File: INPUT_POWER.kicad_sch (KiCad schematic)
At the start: 30 parts, among them J1 TYPE-C-31-M12_13, SW3 ON/OFF, U3 IP5306

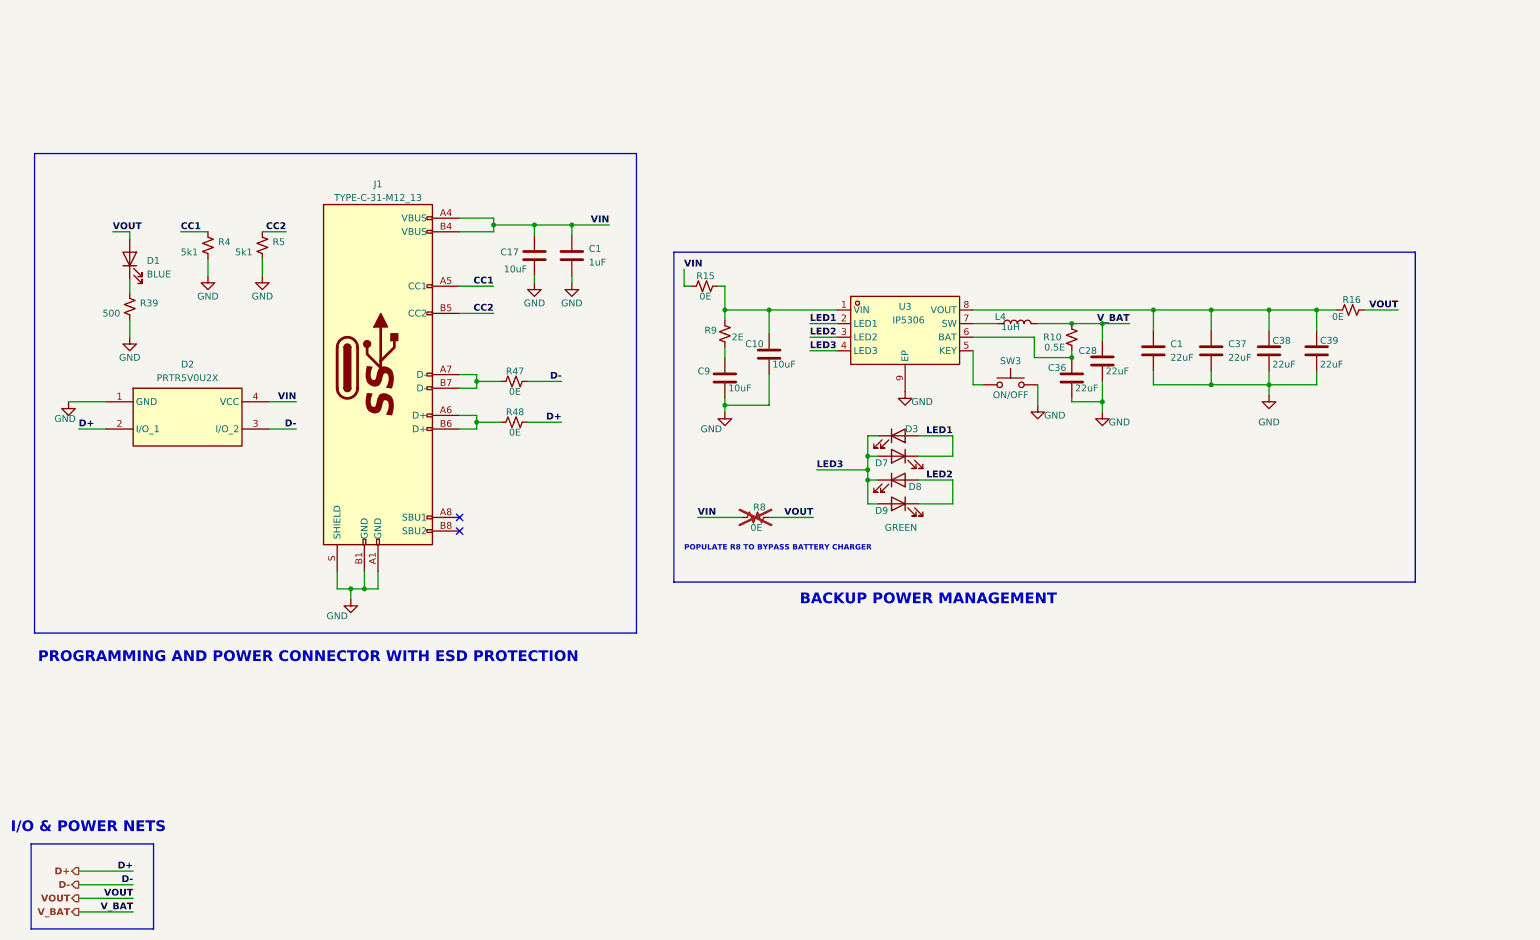
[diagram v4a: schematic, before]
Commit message: Added Arduino style SS for GPIO headers, Added BLE & Wi-Fi symbol
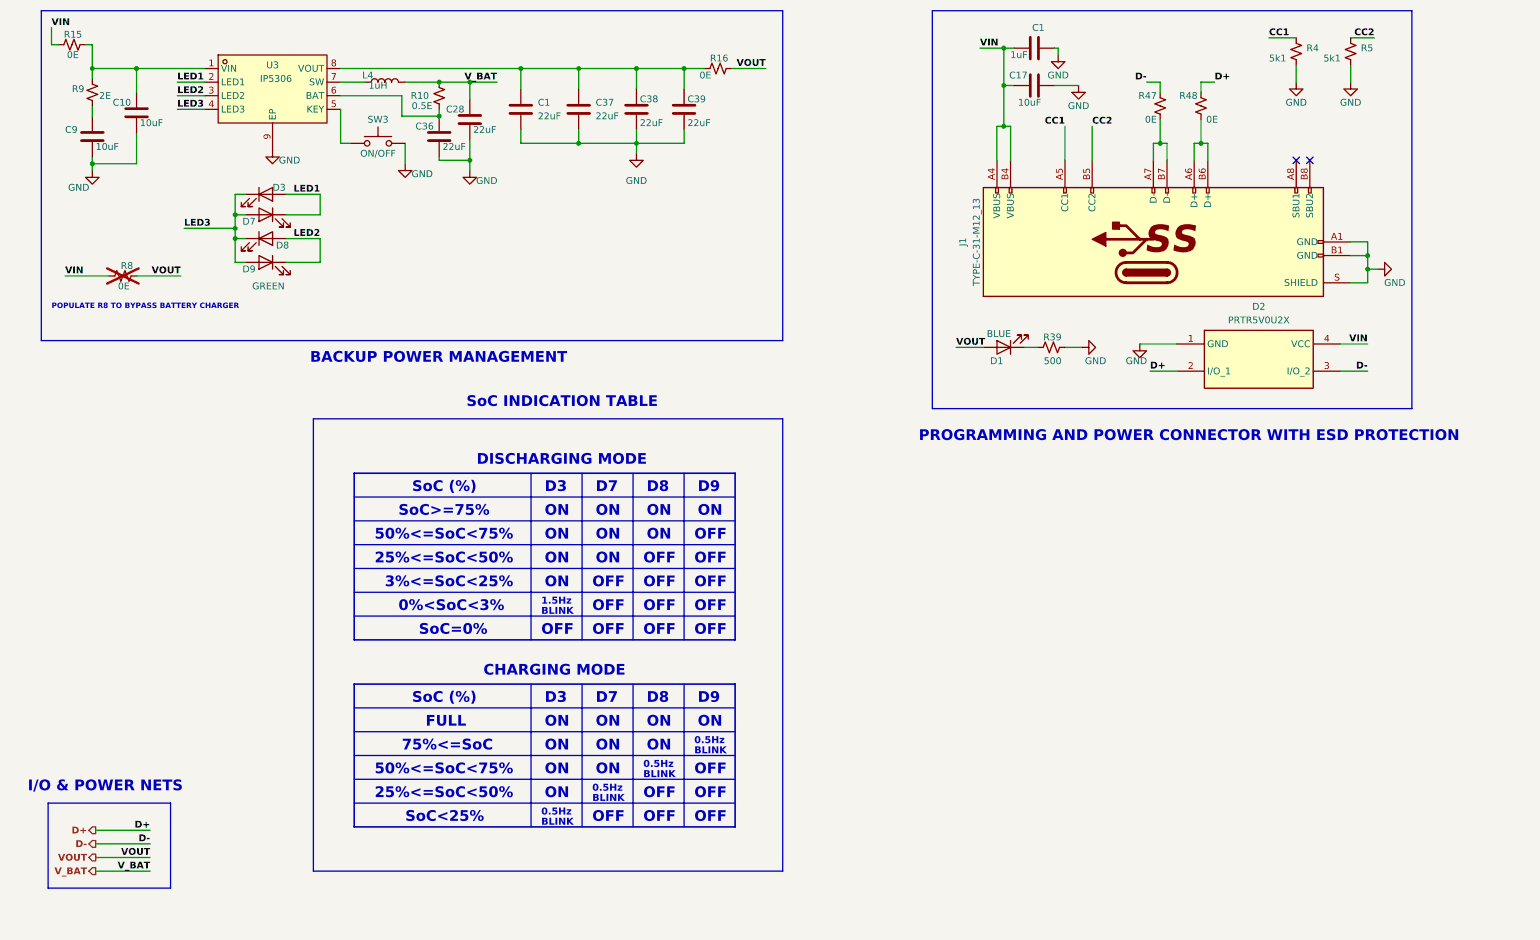
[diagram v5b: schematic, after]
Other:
- note added: "0%<SoC<3%"
- note added: "0.5Hz"
- note added: "1.5Hz"
- note added: "25%<=SoC<50%"
- note added: "3%<=SoC<25%"
- note added: "50%<=SoC<75%"
- note added: "75%<=SoC"
- note added: "BLINK"
- note added: "CHARGING MODE"
- note added: "D3"
- note added: "D7"
- note added: "D8"
- note added: "D9"
- note added: "DISCHARGING MODE"
- note added: "FULL"
- note added: "OFF"
- note added: "ON"
- note added: "SoC (%)"
- note added: "SoC INDICATION TABLE"
- note added: "SoC<25%"
- note added: "SoC=0%"
- note added: "SoC>=75%"
- moved on the sheet: C1, C10, C17, C28, C36, C37, C38, C39, C9, D1, D2, D3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

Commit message: Added HW-Tinkerers logo and supporting graphics
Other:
- company: (none) -> HW-TINKERERS (hw.tinkerers@gmail.com)
- title: (none) -> HARDWARE TINKERERS ESP32-S3 DB
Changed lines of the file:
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@@
 (kicad_sch (version 20230121) (generator eeschema)
   (paper "A4")
+  (title_block
+    (title "HARDWARE TINKERERS ESP32-S3 DB")
+    (rev "1.0.0")
+    (company "HW-TINKERERS (hw.tinkerers@gmail.com)")
+    (comment 1 "Email: bhandarkasrishtikr111@gmail.com")
+    (comment 2 "Author: Srishtik Bhandarkar")
+    (comment 3 "Email: vaibhavkhatri00@gmail.com")
+    (comment 4 "Author: Vaibhav Khatri")
+    (comment 5 "Official HW-Tinkerers email: hw.tinkerers@gmail.com")
+  )
   (junction (at 121.92 41.91) (diameter 0) (color 0 0 0 0)
   )

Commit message: Added production files for JLC (BOM and CPL)
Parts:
- C1: LCSC Part Number (none) -> C14664
- C1, C37, C38, C39: LCSC Part Number (none) -> C12891
- C10, C17, C9: LCSC Part Number (none) -> C15850
- C28, C36: LCSC Part Number (none) -> C2762594
- D1: LCSC Part Number (none) -> C84266
- D2: LCSC Part Number (none) -> C2827688
- D3, D7, D8, D9: LCSC Part Number (none) -> C84264
- L4: LCSC Part Number (none) -> C576540
- R10: LCSC Part Number (none) -> C346785
- R15, R16, R47, R48, R8: LCSC Part Number (none) -> C95177
- R39: LCSC Part Number (none) -> C137970
- R4, R5: LCSC Part Number (none) -> C105872
- R9: LCSC Part Number (none) -> C137886
- SW3: LCSC Part Number (none) -> C92584
- U3: LCSC Part Number (none) -> C181692
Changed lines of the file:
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@@
+      (effects (font (size 1.27 1.27)) hide)
+    )
+    (property "LCSC Part Number" "C14664" (at 207.01 24.13 0)
       (effects (font (size 1.27 1.27)) hide)
     )
@@
       (effects (font (size 1.27 1.27)) hide)
     )
+    (property "LCSC Part Number" "C95177" (at 147.955 27.94 0)
+      (effects (font (size 1.27 1.27)) hide)
+    )
     (pin "1")
     (pin "2")
@@
     )
     (property "PN" "NCD0603C1" (at 63.5 51.435 0)
+      (effects (font (size 1.27 1.27)) hide)
+    )
+    (property "LCSC Part Number" "C84264" (at 63.5 51.435 0)
       (effects (font (size 1.27 1.27)) hide)
     )
@@
       (effects (font (size 1.27 1.27)) hide)
     )
+    (property "LCSC Part Number" "C2827688" (at 233.68 79.375 0)
+      (effects (font (size 1.27 1.27)) hide)
+    )
     (pin "1")
     (pin "2")
@@
       (effects (font (size 1.27 1.27)) hide)
     )
+    (property "LCSC Part Number" "C15850" (at 31.115 40.64 0)
+      (effects (font (size 1.27 1.27)) hide)
+    )
     (pin "1")
     (pin "2")
@@
       (effects (font (size 1.27 1.27)) hide)
     )
+    (property "LCSC Part Number" "C137970" (at 210.185 80.01 0)
+      (effects (font (size 1.27 1.27)) hide)
+    )
     (pin "1")
     (pin "2")
@@
     )
     (property "PN" "CL21A106KAYNNNE" (at 207.01 31.115 0)
+      (effects (font (size 1.27 1.27)) hide)
+    )
+    (property "LCSC Part Number" "C15850" (at 207.01 31.115 0)
       (effects (font (size 1.27 1.27)) hide)
     )
@@
       (effects (font (size 1.27 1.27)) hide)
     )
+    (property "LCSC Part Number" "C84266" (at 201.295 80.01 0)
+      (effects (font (size 1.27 1.27)) hide)
+    )
     (pin "1")
     (pin "2")
@@
     )
     (property "PN" "IP5306" (at 64.77 27.94 0)
+      (effects (font (size 1.27 1.27)) hide)
+    )
+    (property "LCSC Part Number" "C181692" (at 64.77 27.94 0)
       (effects (font (size 1.27 1.27)) hide)
     )
@@
       (effects (font (size 1.27 1.27)) hide)
     )
+    (property "LCSC Part Number" "C2762594" (at 101.6 37.465 0)
+      (effects (font (size 1.27 1.27)) hide)
+    )
     (pin "1")
     (pin "2")
@@
     )
     (property "PN" "CL10A226MO7JZNC" (at 95.885 40.64 0)
+      (effects (font (size 1.27 1.27)) hide)
+    )
+    (property "LCSC Part Number" "C2762594" (at 95.885 40.64 0)
       (effects (font (size 1.27 1.27)) hide)
     )
@@
       (effects (font (size 1.27 1.27)) hide)
     )
+    (property "LCSC Part Number" "C84264" (at 63.5 55.245 0)
+      (effects (font (size 1.27 1.27)) hide)
+    )
     (pin "1")
     (pin "2")
@@
     )
     (property "PN" "CL31A226KAHNNNE" (at 132.715 35.56 0)
+      (effects (font (size 1.27 1.27)) hide)
+    )
+    (property "LCSC Part Number" "C12891" (at 132.715 35.56 0)
       (effects (font (size 1.27 1.27)) hide)
     )
@@
       (effects (font (size 1.27 1.27)) hide)
     )
+    (property "LCSC Part Number" "C346785" (at 95.885 33.02 0)
+      (effects (font (size 1.27 1.27)) hide)
+    )
     (pin "1")
     (pin "2")
@@
       (effects (font (size 1.27 1.27)) hide)
     )
+    (property "LCSC Part Number" "C92584" (at 84.455 41.91 0)
+      (effects (font (size 1.27 1.27)) hide)
+    )
     (pin "1")
     (pin "2")
@@
       (effects (font (size 1.27 1.27)) hide)
     )
+    (property "LCSC Part Number" "C15850" (at 39.37 36.195 0)
+      (effects (font (size 1.27 1.27)) hide)
+    )
     (pin "1")
     (pin "2")
@@
       (effects (font (size 1.27 1.27)) hide)
     )
+    (property "LCSC Part Number" "C105872" (at 255.905 24.765 0)
+      (effects (font (size 1.27 1.27)) hide)
+    )
     (pin "1")
     (pin "2")
@@
       (effects (font (size 1.27 1.27)) hide)
     )
+    (property "LCSC Part Number" "C105872" (at 266.065 24.765 0)
+      (effects (font (size 1.27 1.27)) hide)
+    )
     (pin "1")
     (pin "2")
@@
     )
     (property "PN" "RC0603JR-070RL" (at 238.125 34.925 0)
+      (effects (font (size 1.27 1.27)) hide)
+    )
+    (property "LCSC Part Number" "C95177" (at 238.125 34.925 0)
       (effects (font (size 1.27 1.27)) hide)
     )
@@
     )
     (property "PN" "NCD0603C1" (at 63.5 64.135 0)
+      (effects (font (size 1.27 1.27)) hide)
+    )
+    (property "LCSC Part Number" "C84264" (at 63.5 64.135 0)
       (effects (font (size 1.27 1.27)) hide)
     )
@@
       (effects (font (size 1.27 1.27)) hide)
     )
+    (property "LCSC Part Number" "C95177" (at 36.83 66.675 0)
+      (effects (font (size 1.27 1.27)) hide)
+    )
     (pin "1")
     (pin "2")
@@
       (effects (font (size 1.27 1.27)) hide)
     )
+    (property "LCSC Part Number" "C12891" (at 111.125 35.56 0)
+      (effects (font (size 1.27 1.27)) hide)
+    )
     (pin "1")
     (pin "2")
@@
       (effects (font (size 1.27 1.27)) hide)
     )
+    (property "LCSC Part Number" "C576540" (at 85.725 30.48 0)
+      (effects (font (size 1.27 1.27)) hide)
+    )
     (pin "1")
     (pin "2")
@@
     )
     (property "PN" "NCD0603C1" (at 63.5 59.69 0)
+      (effects (font (size 1.27 1.27)) hide)
+    )
+    (property "LCSC Part Number" "C84264" (at 63.5 59.69 0)
       (effects (font (size 1.27 1.27)) hide)
     )
@@
       (effects (font (size 1.27 1.27)) hide)
     )
+    (property "LCSC Part Number" "C95177" (at 27.305 23.495 0)
+      (effects (font (size 1.27 1.27)) hide)
+    )
     (pin "1")
     (pin "2")
@@
       (effects (font (size 1.27 1.27)) hide)
     )
+    (property "LCSC Part Number" "C95177" (at 230.505 34.925 0)
+      (effects (font (size 1.27 1.27)) hide)
+    )
     (pin "1")
     (pin "2")
@@
     )
     (property "PN" "CL31A226KAHNNNE" (at 141.605 35.56 0)
+      (effects (font (size 1.27 1.27)) hide)
+    )
+    (property "LCSC Part Number" "C12891" (at 141.605 35.56 0)
       (effects (font (size 1.27 1.27)) hide)
     )
@@
       (effects (font (size 1.27 1.27)) hide)
     )
+    (property "LCSC Part Number" "C12891" (at 121.92 35.56 0)
+      (effects (font (size 1.27 1.27)) hide)
+    )
     (pin "1")
     (pin "2")
@@
       (effects (font (size 1.27 1.27)) hide)
     )
+    (property "LCSC Part Number" "C137886" (at 31.115 32.385 0)
+      (effects (font (size 1.27 1.27)) hide)
+    )
